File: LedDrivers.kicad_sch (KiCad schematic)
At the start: 40 parts, among them Q1 HL2309, Q2 HL2309, Q3 HL2309, Q4 HL2309, Q5 HL2309, U1 LTV-5314-TP1, U2 LTV-5314-TP1, U3 LTV-5314-TP1, U4 LTV-5314-TP1, U5 LTV-5314-TP1

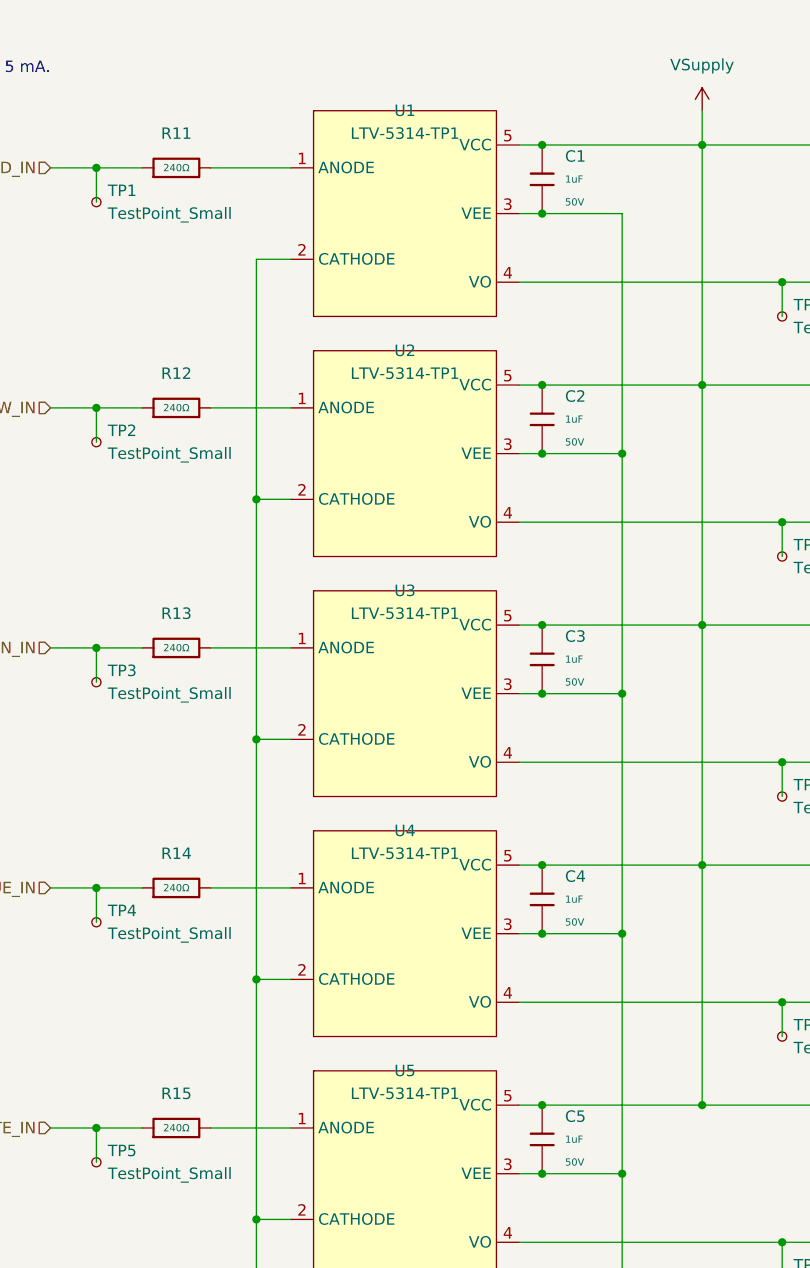
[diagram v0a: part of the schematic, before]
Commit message: Recreated symbol/footprint libraries, added 3D models and Git LFS
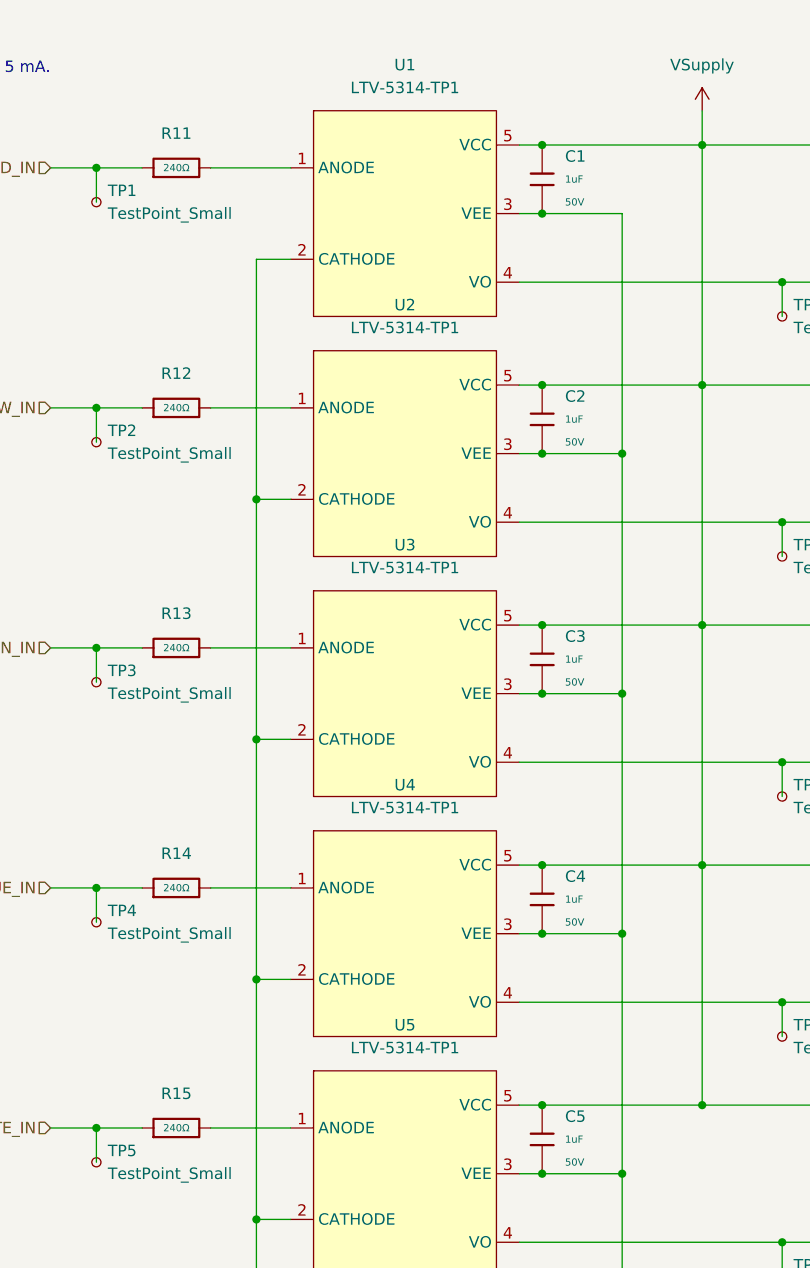
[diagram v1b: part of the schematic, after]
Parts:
- removed U1, U2, U3, U4, U5: LTV-5314-TP1, symbol Custom_symbols:LTV-5314-TP1
- added U1, U2, U3, U4, U5: LTV-5314-TP1, symbol Project_symbols:LTV-5314-TP1
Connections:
- net GND: now also U1.2 (CATHODE), U1.3 (VEE), U2.2 (CATHODE), U2.3 (VEE), U3.2 (CATHODE), U3.3 (VEE), U4.2 (CATHODE), U4.3 (VEE), U5.2 (CATHODE), U5.3 (VEE)
- net VSupply: now also U1.5 (VCC), U2.5 (VCC), U3.5 (VCC), U4.5 (VCC), U5.5 (VCC)
- net at R15.2: now also U5.1 (ANODE)
- net at R20.1, TP10.1: now also U5.4 (VO)
- net at R12.2: now also U2.1 (ANODE)
- net at R17.1, TP7.1: now also U2.4 (VO)
- net at R18.1, TP8.1: now also U3.4 (VO)
- net at R16.1, TP6.1: now also U1.4 (VO)
- net at R11.2: now also U1.1 (ANODE)
- net at R13.2: now also U3.1 (ANODE)
- net at R19.1, TP9.1: now also U4.4 (VO)
- net at R14.2: now also U4.1 (ANODE)

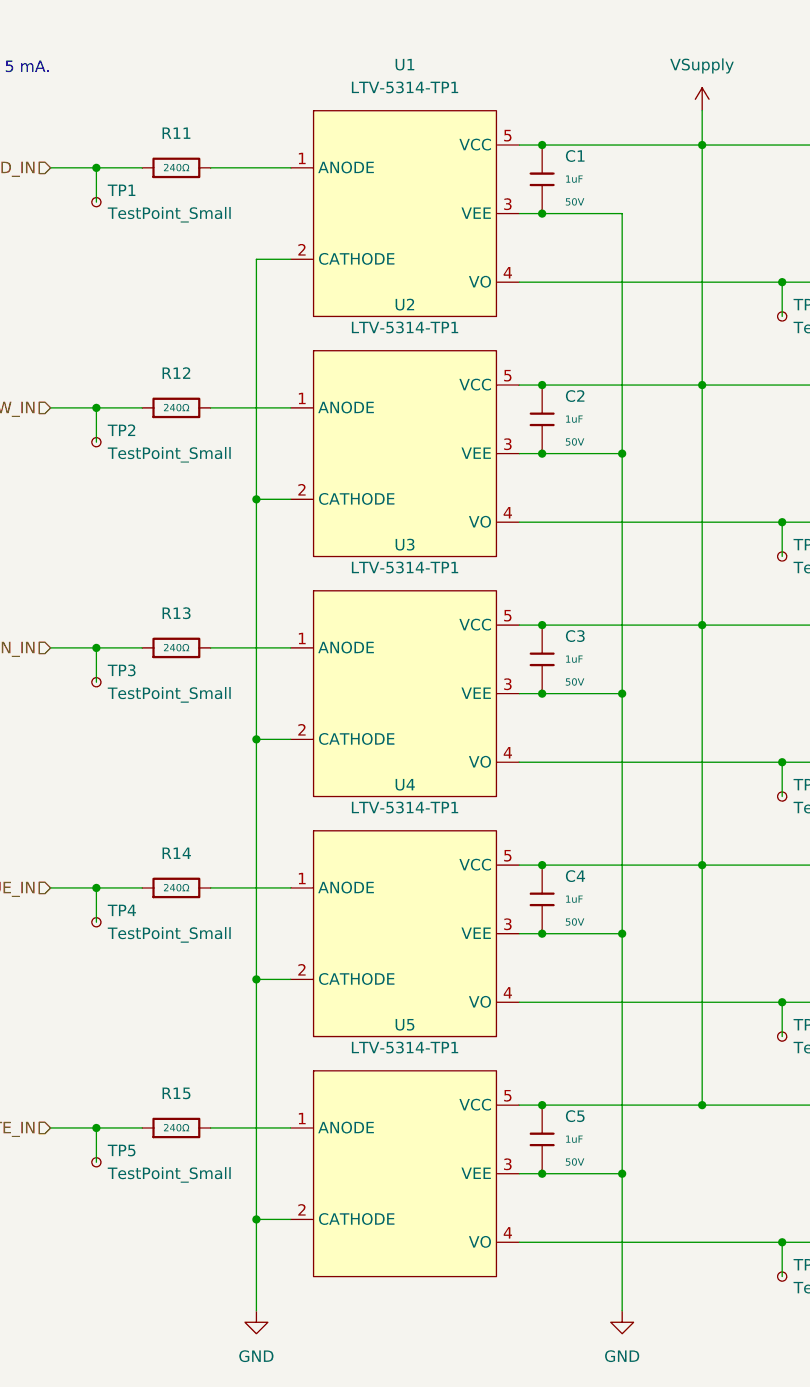
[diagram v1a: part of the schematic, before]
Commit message: Added basic Littelfuse clip model, began laying out PCB
Still needs revisions to TVS diodes.
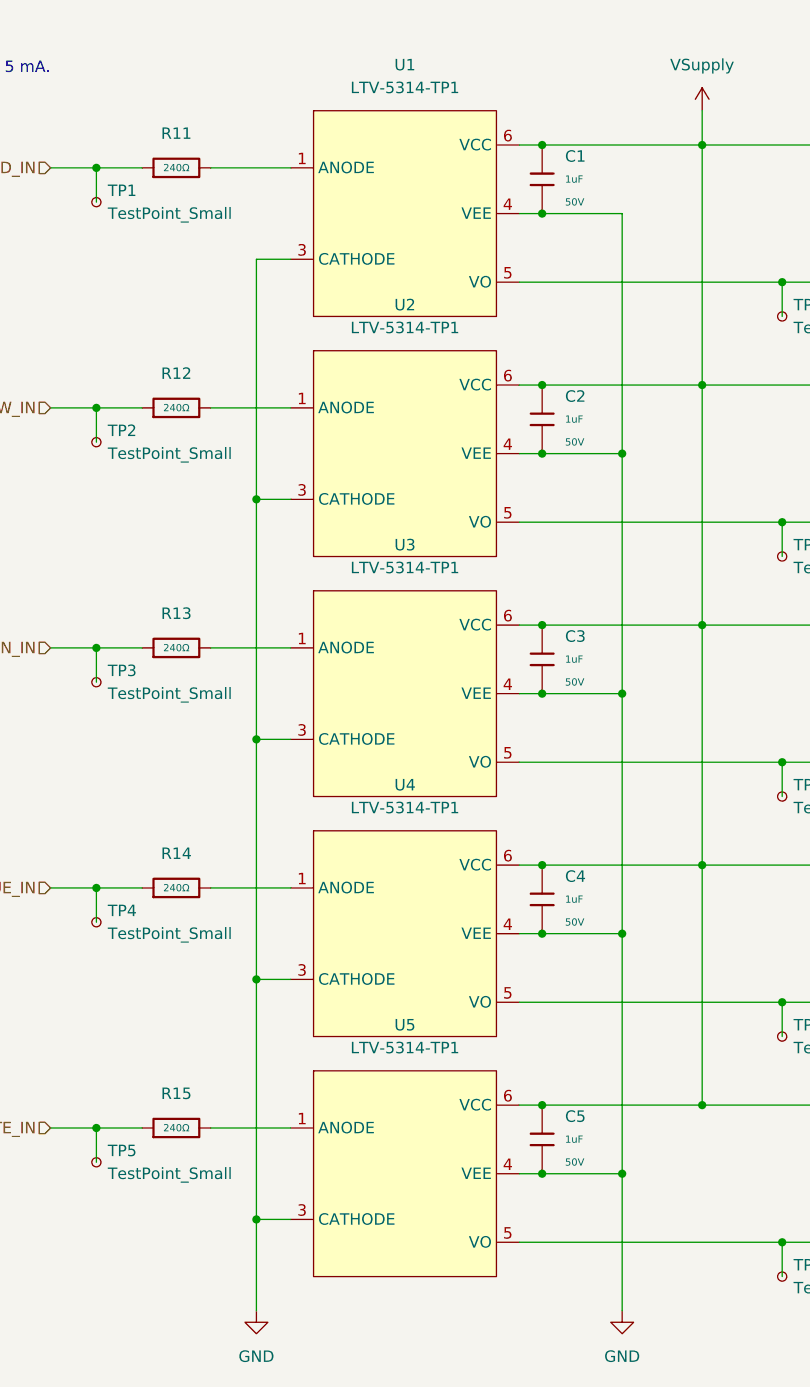
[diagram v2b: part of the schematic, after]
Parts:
- U1, U2, U3, U4, U5: footprint (none) -> Project_footprints:LTV-5314-TP1
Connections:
- net GND: now also U1.4 (VEE), U2.4 (VEE), U3.4 (VEE), U4.4 (VEE), U5.4 (VEE); no longer U1.2 (CATHODE), U2.2 (CATHODE), U3.2 (CATHODE), U4.2 (CATHODE), U5.2 (CATHODE)
- net VSupply: now also U1.6 (VCC), U2.6 (VCC), U3.6 (VCC), U4.6 (VCC), U5.6 (VCC); no longer U1.5 (VCC), U2.5 (VCC), U3.5 (VCC), U4.5 (VCC), U5.5 (VCC)
- net at R17.1, TP7.1: now also U2.5 (VO); no longer U2.4 (VO)
- net at R16.1, TP6.1: now also U1.5 (VO); no longer U1.4 (VO)
- net at R18.1, TP8.1: now also U3.5 (VO); no longer U3.4 (VO)
- net at R20.1, TP10.1: now also U5.5 (VO); no longer U5.4 (VO)
- net at R19.1, TP9.1: now also U4.5 (VO); no longer U4.4 (VO)
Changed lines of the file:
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@@
 	)
 	(symbol
+		(lib_name "LTV-5314-TP1_1")
 		(lib_id "Project_symbols:LTV-5314-TP1")
 		(at 128.27 34.29 0)
@@
 			)
 		)
-		(property "Footprint" ""
+		(property "Footprint" "Project_footprints:LTV-5314-TP1"
 			(at 128.27 34.29 0)
 			(effects
@@
 			)
 		)
-		(pin "2"
+		(pin "6"
 		)
 		(pin "1"
@@
 			)
 		)
-		(property "Footprint" ""
+		(property "Footprint" "Project_footprints:LTV-5314-TP1"
 			(at 128.27 140.97 0)
 			(effects
@@
 			)
 		)
-		(pin "2"
+		(pin "6"
 		)
 		(pin "1"
@@
 	)
 	(symbol
+		(lib_name "LTV-5314-TP1_3")
 		(lib_id "Project_symbols:LTV-5314-TP1")
 		(at 128.27 87.63 0)
@@
 			)
 		)
-		(property "Footprint" ""
+		(property "Footprint" "Project_footprints:LTV-5314-TP1"
 			(at 128.27 87.63 0)
 			(effects
@@
 			)
 		)
-		(pin "2"
+		(pin "6"
 		)
 		(pin "1"
@@
 	)
 	(symbol
+		(lib_name "LTV-5314-TP1_2")
 		(lib_id "Project_symbols:LTV-5314-TP1")
 		(at 128.27 60.96 0)
@@
 			)
 		)
-		(property "Footprint" ""
+		(property "Footprint" "Project_footprints:LTV-5314-TP1"
 			(at 128.27 60.96 0)
 			(effects
@@
 			)
 		)
-		(pin "2"
+		(pin "6"
 		)
 		(pin "1"
@@
 	)
 	(symbol
+		(lib_name "LTV-5314-TP1_4")
 		(lib_id "Project_symbols:LTV-5314-TP1")
 		(at 128.27 114.3 0)
@@
 			)
 		)
-		(property "Footprint" ""
+		(property "Footprint" "Project_footprints:LTV-5314-TP1"
 			(at 128.27 114.3 0)
 			(effects
@@
 			)
 		)
-		(pin "2"
+		(pin "6"
 		)
 		(pin "1"

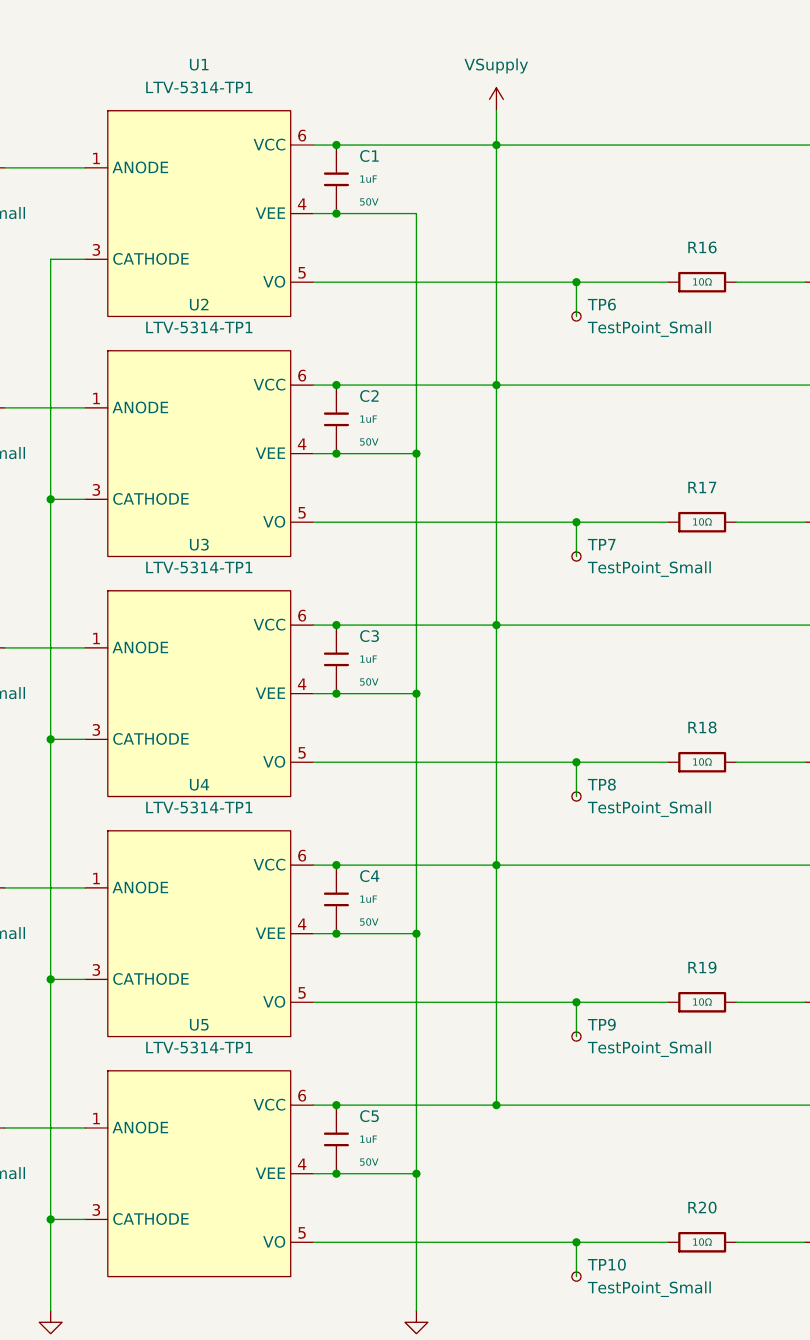
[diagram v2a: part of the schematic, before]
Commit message: Fixed incorrect decoupling capacitance on LTV5314
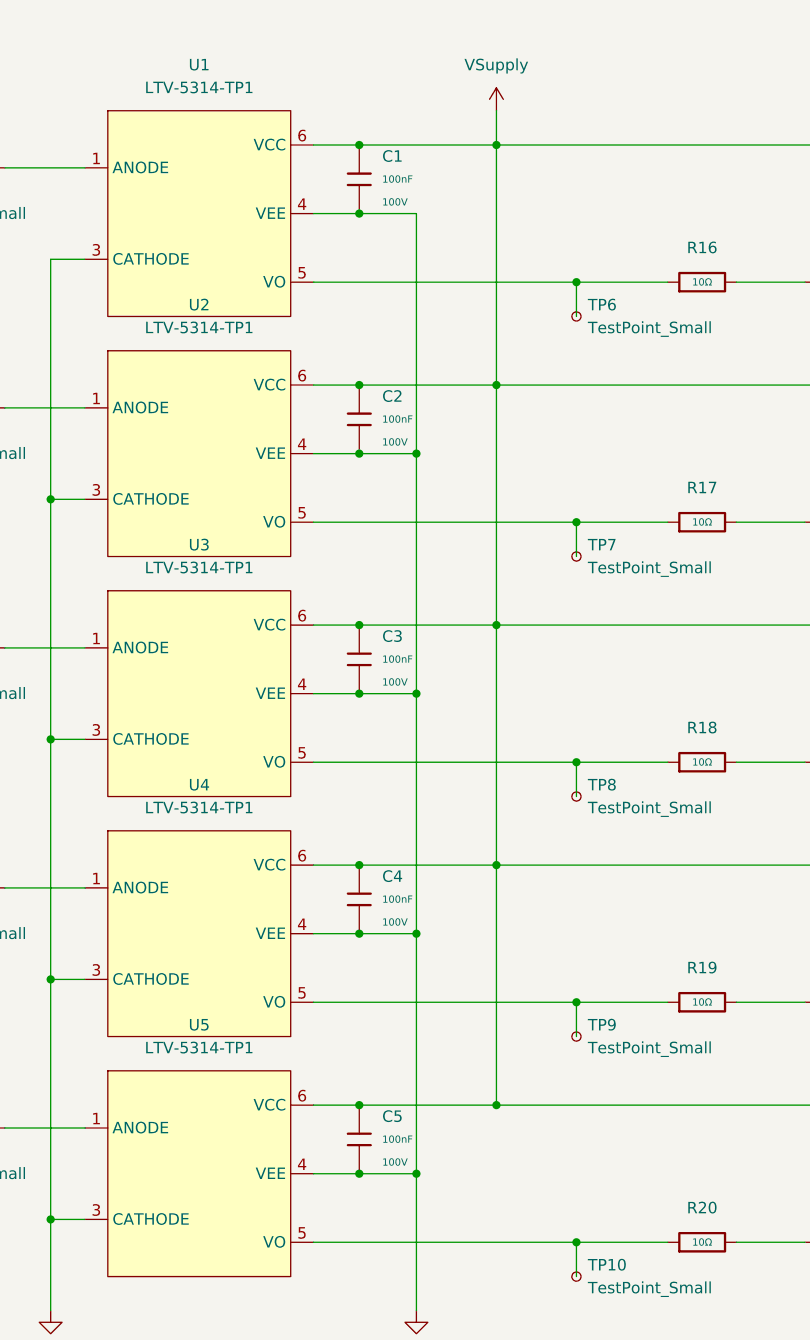
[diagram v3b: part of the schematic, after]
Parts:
- removed C1, C2, C3, C4, C5: 1uF, PCM_JLCPCB:C_0603, symbol PCM_JLCPCB-Capacitors:0603,1uF
- added C1, C2, C3, C4, C5: 100nF, PCM_JLCPCB:C_0805, symbol PCM_JLCPCB-Capacitors:0805,100nF
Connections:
- net GND: now also C1.2, C2.2, C3.2, C4.2, C5.2
- net VSupply: now also C1.1, C2.1, C3.1, C4.1, C5.1
